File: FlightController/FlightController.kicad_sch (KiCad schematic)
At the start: 1 part, among them J1 GPIO

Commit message: Design Schematic
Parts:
- removed J1: GPIO, Connector_PinSocket_2.54mm:PinSocket_2x20_P2.54mm_Vertical, symbol Connector_Generic:Conn_02x20_Odd_Even
- added BZ1: CEM-1201S, Buzzer_Beeper:MagneticBuzzer_ProSignal_ABT-410-RC, symbol Device:Buzzer
- added C1, C2, C7: 0µ1, Capacitor_SMD:C_0805_2012Metric_Pad1.18x1.45mm_HandSolder, symbol Device:C
- added C10: 0µ1, Capacitor_SMD:C_0805_2012Metric_Pad1.18x1.45mm_HandSolder, symbol Device:C_Small
- added C11, C4, C5, C6: 22µ, Capacitor_SMD:C_0805_2012Metric_Pad1.18x1.45mm_HandSolder, symbol Device:C
- added C3: 22µ, Capacitor_SMD:C_0805_2012Metric_Pad1.18x1.45mm_HandSolder, symbol Device:C_Small
- added C8: 10p, Capacitor_SMD:C_0805_2012Metric_Pad1.18x1.45mm_HandSolder, symbol Device:C_Small
- added C9: 1µ, Capacitor_SMD:C_0805_2012Metric_Pad1.18x1.45mm_HandSolder, symbol Device:C
- added D1, D2: 1N4148W, Diode_SMD:D_SOD-123, symbol Diode:1N4148W
- added H1, H2, H3, H4: MountingHole_Pad, MountingHole:MountingHole_3.2mm_M3_DIN965_Pad_TopBottom, symbol Mechanical:MountingHole_Pad
- added H5: MountingHole_Pad, MountingHole:MountingHole_2.2mm_M2_DIN965_Pad_TopBottom, symbol Mechanical:MountingHole_Pad
- added J1: Conn_01x06, Connector_PinHeader_2.54mm:PinHeader_1x06_P2.54mm_Vertical, symbol Connector_Generic:Conn_01x06
- added J2: USB_C_Receptacle_USB2.0_14P, Connector_USB:USB_C_Receptacle_HRO_TYPE-C-31-M-12, symbol Connector:USB_C_Receptacle_USB2.0_14P
- added J3: Conn_01x02, Connector_PinHeader_2.54mm:PinHeader_1x02_P2.54mm_Vertical, symbol Connector_Generic:Conn_01x02
- added J4: 60312002114503, Connector_Coaxial:SMA_Wurth_60312002114503_Vertical, symbol Connector:Conn_Coaxial_Small
- added JP1: Power Save, Jumper:SolderJumper-3_P1.3mm_Bridged12_RoundedPad1.0x1.5mm, symbol Jumper:SolderJumper_3_Bridged12
- added L1: 1µH, Inductor_SMD:L_Coilcraft_XxL4020, symbol Device:L
- added NT1, NT2, NT3: NetTie_2, NetTie:NetTie-2_SMD_Pad0.5mm, symbol Device:NetTie_2
- added Q1: Si2338DS, Package_TO_SOT_SMD:SOT-23, symbol Simulation_SPICE:NMOS
- added Q2: SI2347DS, Package_TO_SOT_SMD:SOT-23, symbol Simulation_SPICE:PMOS
- added R1, R4, R6: 10k, Resistor_SMD:R_0805_2012Metric_Pad1.20x1.40mm_HandSolder, symbol Device:R
- added R10, R9: 120k, Resistor_SMD:R_0805_2012Metric_Pad1.20x1.40mm_HandSolder, symbol Device:R
- added R11, R12: 5k1, Resistor_SMD:R_0805_2012Metric_Pad1.20x1.40mm_HandSolder, symbol Device:R_Small
- added R2: 100k, Resistor_SMD:R_0805_2012Metric_Pad1.20x1.40mm_HandSolder, symbol Device:R
- added R3: 220k, Resistor_SMD:R_0805_2012Metric_Pad1.20x1.40mm_HandSolder, symbol Device:R
- added R5: 1M, Resistor_SMD:R_0805_2012Metric_Pad1.20x1.40mm_HandSolder, symbol Device:R_Small
- added R7: 1M, Resistor_SMD:R_0805_2012Metric_Pad1.20x1.40mm_HandSolder, symbol Device:R
- added R8: 180k, Resistor_SMD:R_0805_2012Metric_Pad1.20x1.40mm_HandSolder, symbol Device:R_Small
- added SW1: SW_SPST, htl_smd:SW_Push_5.1mm_H1.5mm, symbol Switch:SW_SPST
- added SW2: SW_SPST, Connector_PinHeader_2.54mm:PinHeader_1x02_P2.54mm_Vertical, symbol Switch:SW_SPST
- added TP1: TestPoint, TestPoint:TestPoint_Pad_D1.0mm, symbol Connector:TestPoint
- added U1, U4, U6: BME680, Package_LGA:Bosch_LGA-8_3x3mm_P0.8mm_ClockwisePinNumbering, symbol Sensor:BME680
- added U2: ESP32-S3-MINI-1, RF_Module:ESP32-S2-MINI-1, symbol RF_Module:ESP32-S3-MINI-1
- added U3: TPS63060, Package_SON:Texas_DSC0010J_ThermalVias, symbol Regulator_Switching:TPS63060
- added U5: NEO-M9N, RF_GPS:ublox_NEO, symbol RF_GPS:NEO-M9N
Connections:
- net +3V3: now also J1.6 (Pin_6), NT2.2, R1.2, R10.2, U1.6 (VDDIO), U1.8 (VDD), U2.3 (3V3), U4.6 (VDDIO), U4.8 (VDD), U6.6 (VDDIO), U6.8 (VDD)
- net GND: now also C1.2, C10.2, C11.2, C2.2, C3.2, C4.2, C5.2, C6.2, C7.2, C8.2, C9.2, H1.1, H2.1, H3.1, H4.1, H5.1, J1.1 (Pin_1), J2.A1 (GND), J2.A12 (GND), J2.B1 (GND), J2.B12 (GND), J2.SH (SHIELD), J3.1 (Pin_1), J4.2 (Ext), JP1.1 (A), Q1.3 (S), R11.2, R12.2, R3.2, R8.2, R9.1, SW1.1 (A), U1.1 (GND), U1.7 (GND), U2.1 (GND), U2.2 (GND), U2.42 (GND), U2.43 (GND), U2.46 (GND), U2.47 (GND), U2.48 (GND), U2.49 (GND), U2.50 (GND), U2.51 (GND), U2.52 (GND), U2.53 (GND), U2.54 (GND), U2.55 (GND), U2.56 (GND), U2.57 (GND), U2.58 (GND), U2.59 (GND), U2.60 (GND), U2.61 (GND), U2.62 (GND), U2.63 (GND), U2.64 (GND), U2.65 (GND), U2.7 (IO3), U3.11 (PGND), U3.7 (GND), U4.1 (GND), U4.7 (GND), U5.10 (GND), U5.12 (GND), U5.13 (GND), U5.2 (D_SEL), U5.24 (GND), U5.7 (VDD_USB), U6.1 (GND), U6.7 (GND)
- new net: SW1.2 (B), U2.4 (IO0)
- new net: C3.1, NT1.1, U3.2 (VIN)
- new net: J2.A5 (CC1), R11.1
- new net: D1.2 (A), R4.1, R6.1, R9.2
- new net: C7.1, D1.1 (K), R6.2, U3.3 (EN)
- new net: D2.2 (A), J2.A4 (VBUS), J2.A9 (VBUS), J2.B4 (VBUS), J2.B9 (VBUS)
- new net: J2.B5 (CC2), R12.1
- new net: Q2.1 (D), R10.1, U6.2 (CSB)
- new net: C4.1, C5.1, C6.1, NT2.1, R5.1, R7.1, U3.9 (VOUT)
- new net: C8.1, R5.2, R8.1, U3.8 (FB)
- new net: BZ1.2 (-), Q1.1 (D)
- new net: C1.1, R1.1, U2.45 (EN)
- new net: J4.1 (In), U5.11 (RF_IN)
- new net: JP1.2 (C), U3.4 (PS/SYNC)
- new net: C10.1, U3.6 (VAUX)
- new net: R4.2, SW2.1 (A)
- new net: C9.1, NT3.1, U5.22 (V_BCKP), U5.23 (VCC)
- new net: TP1.1, U5.1 (~{SAFEBOOT})
- new net: L1.1, U3.1 (L1)
- new net: L1.2, U3.10 (L2)
- new net +3.3V: NT3.2
- new net +BATT: BZ1.1 (+), C11.1, D2.1 (K), J3.2 (Pin_2), JP1.3 (B), NT1.2, R2.1, SW2.2 (B)
- new net BUZZER: Q1.2 (G), U2.18 (IO14)
- new net CHARGE: C2.1, R2.2, R3.1, U2.8 (IO4)
- new net CSB0: U1.2 (CSB), U2.14 (IO10)
- new net CSB1: U2.13 (IO9), U4.2 (CSB)
- new net CSB2: Q2.3 (S), U2.12 (IO8)
- new net CSB3: U2.11 (IO7), U5.18 (SDA/~{SPI_CS})
- new net CSB4: J1.2 (Pin_2), U2.10 (IO6)
- new net D+: J2.A6 (D+), J2.B6 (D+), U2.24 (USB_D+)
- new net D-: J2.A7 (D-), J2.B7 (D-), U2.23 (USB_D-)
- new net FAULT: Q2.2 (G), U2.6 (IO2)
- new net MISO: J1.5 (Pin_5), U1.5 (SDO), U2.17 (IO13), U4.5 (SDO), U5.20 (TXD/SPI_MISO), U6.5 (SDO)
- new net MOSI: J1.3 (Pin_3), U1.3 (SDI), U2.15 (IO11), U4.3 (SDI), U5.21 (RXD/SPI_MOSI), U6.3 (SDI)
- new net PG: R7.2, U2.5 (IO1), U3.5 (PG)
- new net SCK: J1.4 (Pin_4), U1.4 (SCK), U2.16 (IO12), U4.4 (SCK), U5.19 (SCL/SPI_CLK), U6.4 (SCK)
- new net ~{GPS_RESET}: U2.9 (IO5), U5.8 (~{RESET})
- no-connect marks 0 -> 28
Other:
- note added: "+BATT zu +3V3 Converter"
- note added: "Akku"
- note added: "Battery"
- note added: "Battery Charge Meter"
- note added: "Buzzer"
- note added: "ESP32"
- note added: "Funk Modul"
- note added: "GPS"
- note added: "Gas, Druck, Temperatur -und Feuchtigkeitssensor 0"
- note added: "Gas, Druck, Temperatur -und Feuchtigkeitssensor 1"
- note added: "Gas, Druck, Temperatur -und Feuchtigkeitssensor 2 + Fehler"
- note added: "Hauptschalter"
- note added: "Mounting"
- note added: "Spule zu Funk Abschirmen!"
- note added: "Spulen- abschirmung"
- note added: "USB C"
- note removed: "Additional pin functions: https://pinout.xyz/"

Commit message: Add Battery Connector Footprint
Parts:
- J3: footprint Connector_PinHeader_2.54mm:PinHeader_1x02_P2.54mm_Vertical -> Connector_Battery:JST-PH-2
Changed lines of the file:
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@@
 			)
 		)
-		(property "Footprint" "Connector_PinHeader_2.54mm:PinHeader_1x02_P2.54mm_Vertical"
+		(property "Footprint" "Connector_Battery:JST-PH-2"
 			(at 130.81 185.42 0)
 			(hide yes)

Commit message: Fix wrong power symbol
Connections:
- net +3.3V is gone; now on net +3V3: NT3.2
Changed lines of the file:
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@@
 	(symbol
 		(lib_id "power:+3V3")
+		(at 247.65 21.59 0)
+		(unit 1)
+		(body_style 1)
+		(exclude_from_sim no)
+		(in_bom yes)
+		(on_board yes)
+		(in_pos_files yes)
+		(dnp no)
+		(fields_autoplaced yes)
+		(property "Reference" "#PWR017"
+			(at 247.65 25.4 0)
+			(hide yes)
+			(show_name no)
+			(do_not_autoplace no)
+			(effects
+				(font
+					(size 1.27 1.27)
+				)
+			)
+		)
+		(property "Value" "+3V3"
+			(at 247.65 16.51 0)
+			(show_name no)
+			(do_not_autoplace no)
+			(effects
+				(font
+					(size 1.27 1.27)
+				)
+			)
+		)
+		(property "Footprint" "Package_LCC:PLCC-84_29.3x29.3mm_P1.27mm"
+			(at 247.65 21.59 0)
+			(hide yes)
+			(show_name no)
+			(do_not_autoplace no)
+			(effects
+				(font
+					(size 1.27 1.27)
+				)
+			)
+		)
+		(property "Datasheet" ""
+			(at 247.65 21.59 0)
+			(hide yes)
+			(show_name no)
+			(do_not_autoplace no)
+			(effects
+				(font
+					(size 1.27 1.27)
+				)
+			)
+		)
+		(property "Description" "Power symbol creates a global label with name \"+3V3\""
+			(at 247.65 21.59 0)
+			(hide yes)
+			(show_name no)
+			(do_not_autoplace no)
+			(effects
+				(font
+					(size 1.27 1.27)
+				)
+			)
+		)
+		(pin "1"
+		)
+		(instances
+			(project "FlightController"
+				(path "/e63e39d7-6ac0-4ffd-8aa3-1841a4541b55"
+					(reference "#PWR017")
+					(unit 1)
+				)
+			)
+		)
+	)
+	(symbol
+		(lib_id "power:+3V3")
 		(at 33.02 149.86 0)
 		(unit 1)
@@
 					(unit 1)
 				)
-			)
-		)
-	)
-	(symbol
-		(lib_id "power:+3.3V")
-		(at 247.65 21.59 0)
-		(unit 1)
-		(body_style 1)
-		(exclude_from_sim no)
-		(in_bom yes)
-		(on_board yes)
-		(in_pos_files yes)
-		(dnp no)
-		(fields_autoplaced yes)
-		(property "Reference" "#PWR017"
-			(at 247.65 25.4 0)
-			(hide yes)
-			(show_name no)
-			(do_not_autoplace no)
-			(effects
-				(font
-					(size 1.27 1.27)
-				)
-			)
-		)
-		(property "Value" "+3.3V"
-			(at 247.65 16.51 0)
-			(show_name no)
-			(do_not_autoplace no)
-			(effects
-				(font
-					(size 1.27 1.27)
-				)
-			)
-		)
-		(property "Footprint" ""
-			(at 247.65 21.59 0)
-			(hide yes)
-			(show_name no)
-			(do_not_autoplace no)
-			(effects
-				(font
-					(size 1.27 1.27)
-				)
-			)
-		)
-		(property "Datasheet" ""
-			(at 247.65 21.59 0)
-			(hide yes)
-			(show_name no)
-			(do_not_autoplace no)
-			(effects
-				(font
-					(size 1.27 1.27)
-				)
-			)
-		)
-		(property "Description" "Power symbol creates a global label with name \"+3.3V\""
-			(at 247.65 21.59 0)
-			(hide yes)
-			(show_name no)
-			(do_not_autoplace no)
-			(effects
-				(font
-					(size 1.27 1.27)
-				)
-			)
-		)
-		(pin "1"
-		)
-		(instances
-			(project "FlightController"
-				(path "/e63e39d7-6ac0-4ffd-8aa3-1841a4541b55"
-					(reference "#PWR017")
-					(unit 1)
-				)

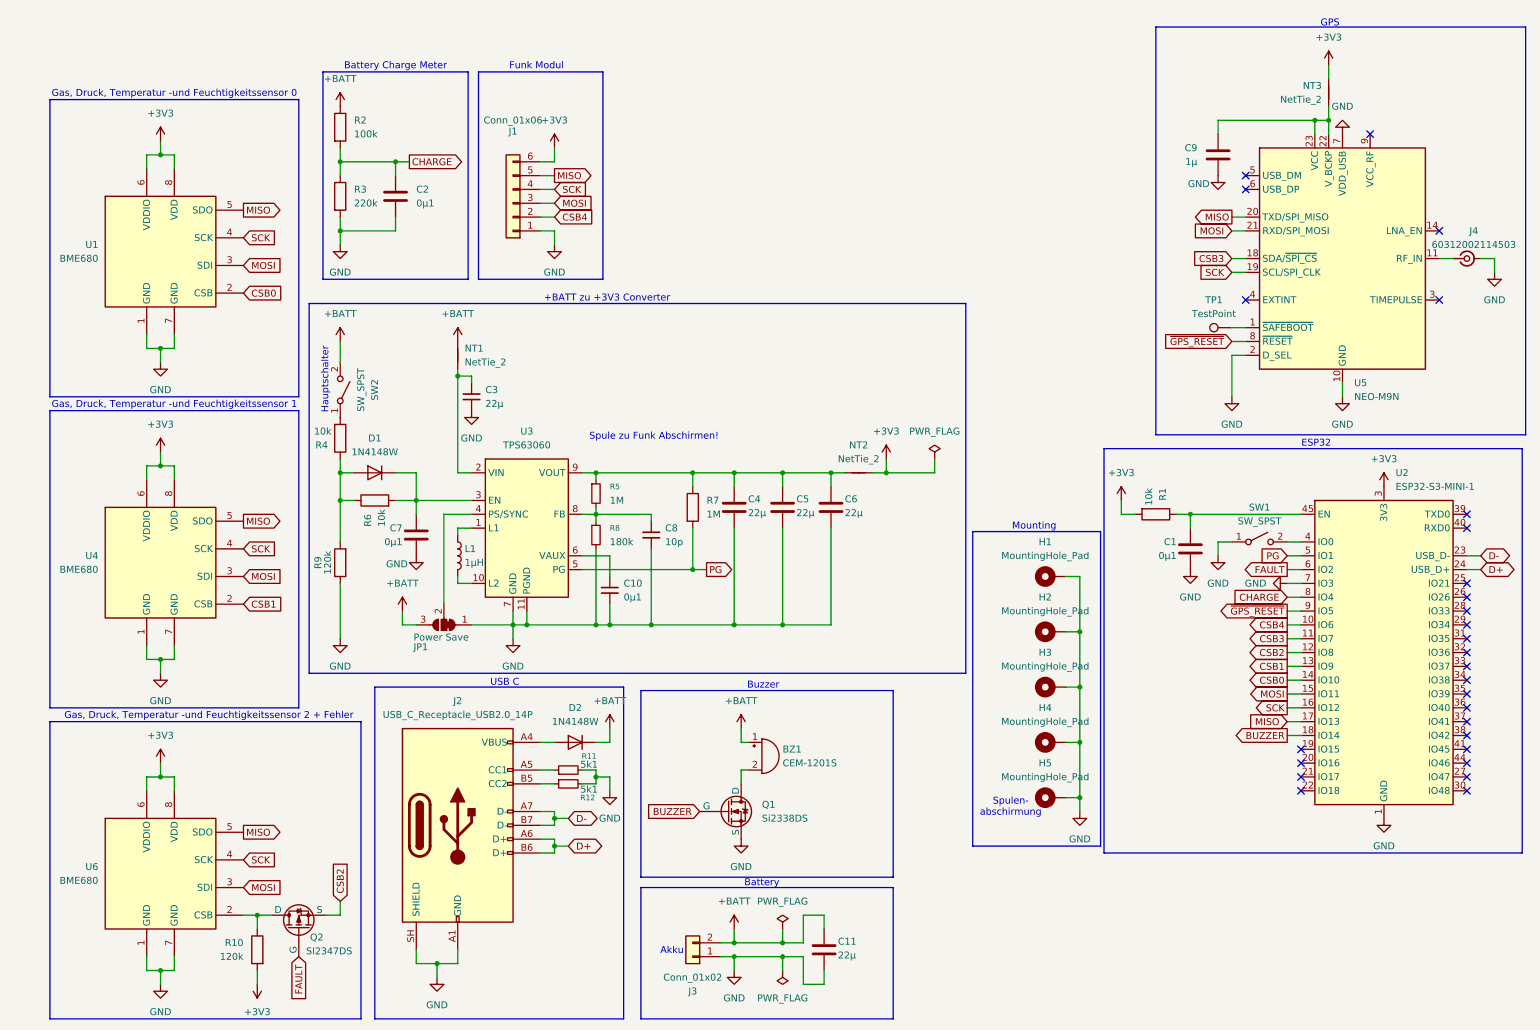
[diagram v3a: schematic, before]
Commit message: Add Power OR and decoupling capacitors
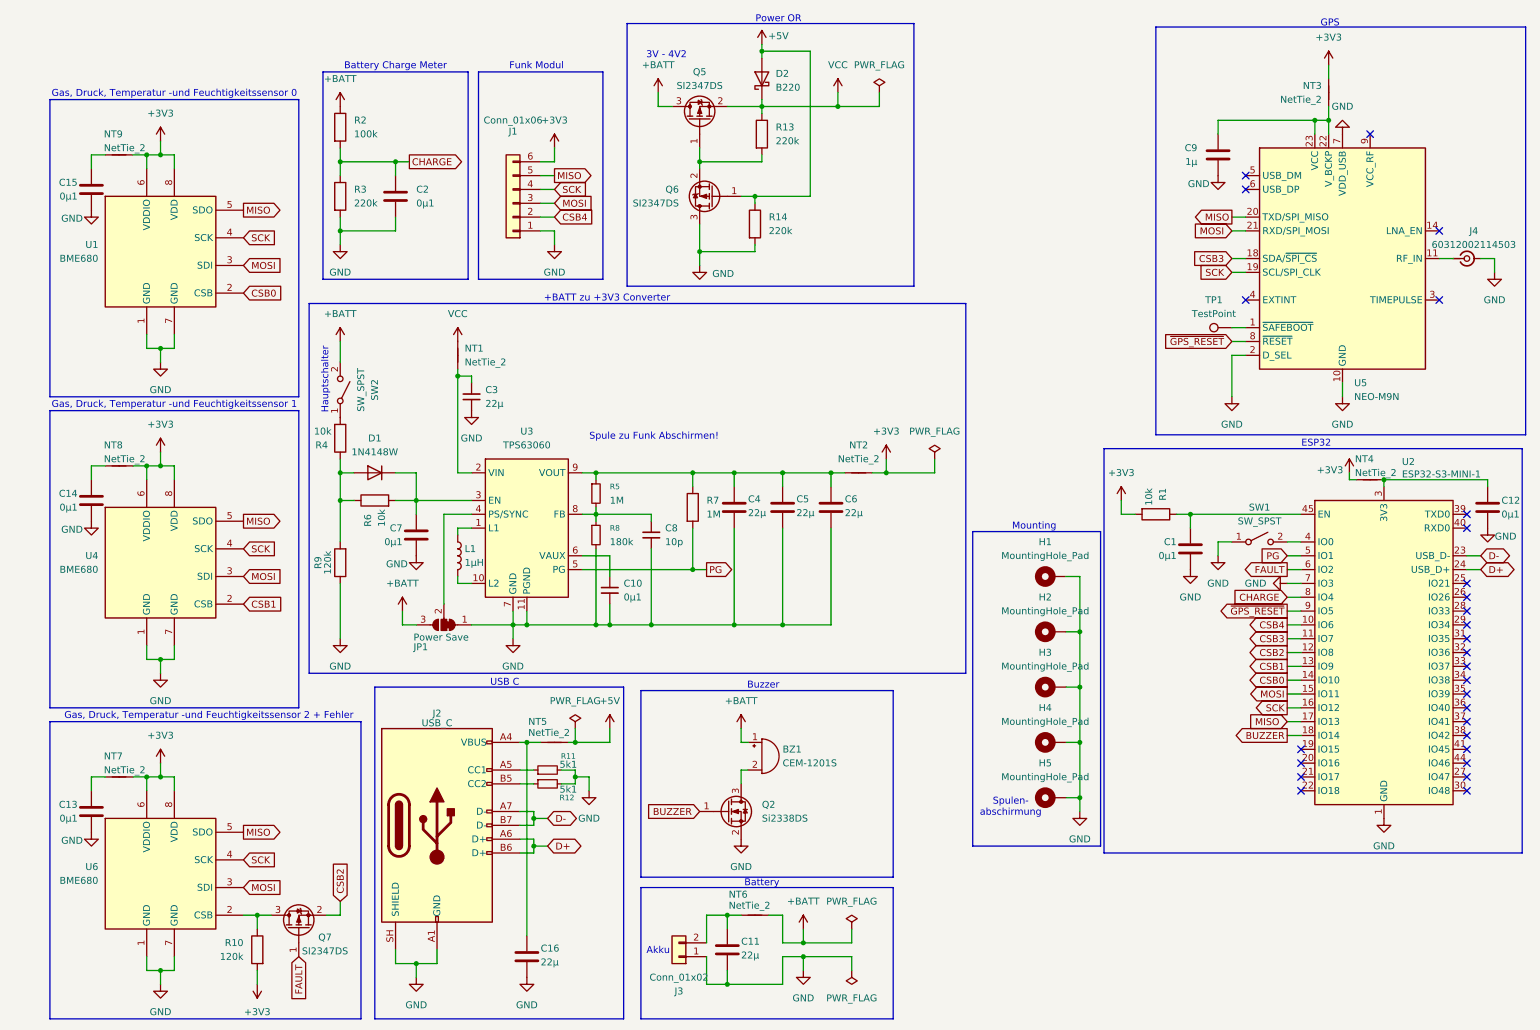
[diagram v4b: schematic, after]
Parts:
- removed D2: 1N4148W, Diode_SMD:D_SOD-123, symbol Diode:1N4148W
- removed Q1: Si2338DS, Package_TO_SOT_SMD:SOT-23, symbol Simulation_SPICE:NMOS
- removed Q2: SI2347DS, Package_TO_SOT_SMD:SOT-23, symbol Simulation_SPICE:PMOS
- added C12, C13, C14, C15: 0µ1, Capacitor_SMD:C_0805_2012Metric_Pad1.18x1.45mm_HandSolder, symbol Device:C
- added C16: 22µ, Capacitor_SMD:C_0805_2012Metric_Pad1.18x1.45mm_HandSolder, symbol Device:C
- added D2: B220, Diode_SMD:D_SMB, symbol Diode:B220
- added NT4, NT7, NT8, NT9: NetTie_2, NetTie:NetTie-2_SMD_Pad0.5mm, symbol Device:NetTie_2
- added NT5, NT6: NetTie_2, NetTie:NetTie-2_SMD_Pad2.0mm, symbol Device:NetTie_2
- added Q2: Si2338DS, Package_QFP:TQFP-44_10x10mm_P0.8mm, symbol Transistor_FET:Q_NMOS_GSD
- added Q5, Q6, Q7: SI2347DS, Package_TO_SOT_SMD:SOT-23, symbol Transistor_FET:Si2319CDS
- added R13, R14: 220k, symbol Device:R
- J2: value USB_C_Receptacle_USB2.0_14P -> USB_C
- NT1, NT2: footprint NetTie:NetTie-2_SMD_Pad0.5mm -> NetTie:NetTie-2_SMD_Pad2.0mm
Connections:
- net +3V3: now also NT4.1, NT7.2, NT8.2, NT9.2; no longer U2.3 (3V3)
- net +BATT: now also NT6.2, Q5.3 (D); no longer C11.1, J3.2 (Pin_2), NT1.2
- net BUZZER: now also Q2.1 (G)
- net CSB2: now also Q7.2 (S)
- net FAULT: now also Q7.1 (G)
- net GND: now also C12.2, C13.2, C14.2, C15.2, C16.2, Q2.2 (S), Q6.3 (D), R14.2
- net at J2.A4 (VBUS), J2.A9 (VBUS), J2.B4 (VBUS)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: now also C16.1, NT5.1
- net at R10.1, U6.2 (CSB): now also Q7.3 (D)
- net at BZ1.2 (-): now also Q2.3 (D)
- new net: C11.1, J3.2 (Pin_2), NT6.1
- new net: C12.1, NT4.2, U2.3 (3V3)
- new net: C13.1, NT7.1
- new net: C14.1, NT8.1
- new net: C15.1, NT9.1
- new net: Q5.1 (G), Q6.2 (S), R13.2
- new net +5V: D2.2 (A), NT5.2, Q6.1 (G), R14.1
- new net VCC: D2.1 (K), NT1.2, Q5.2 (S), R13.1
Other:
- note added: "3V - 4V2"
- note added: "Power OR"
- moved on the sheet: C11, J2, J3, R11, R12
